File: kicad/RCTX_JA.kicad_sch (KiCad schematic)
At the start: 48 parts

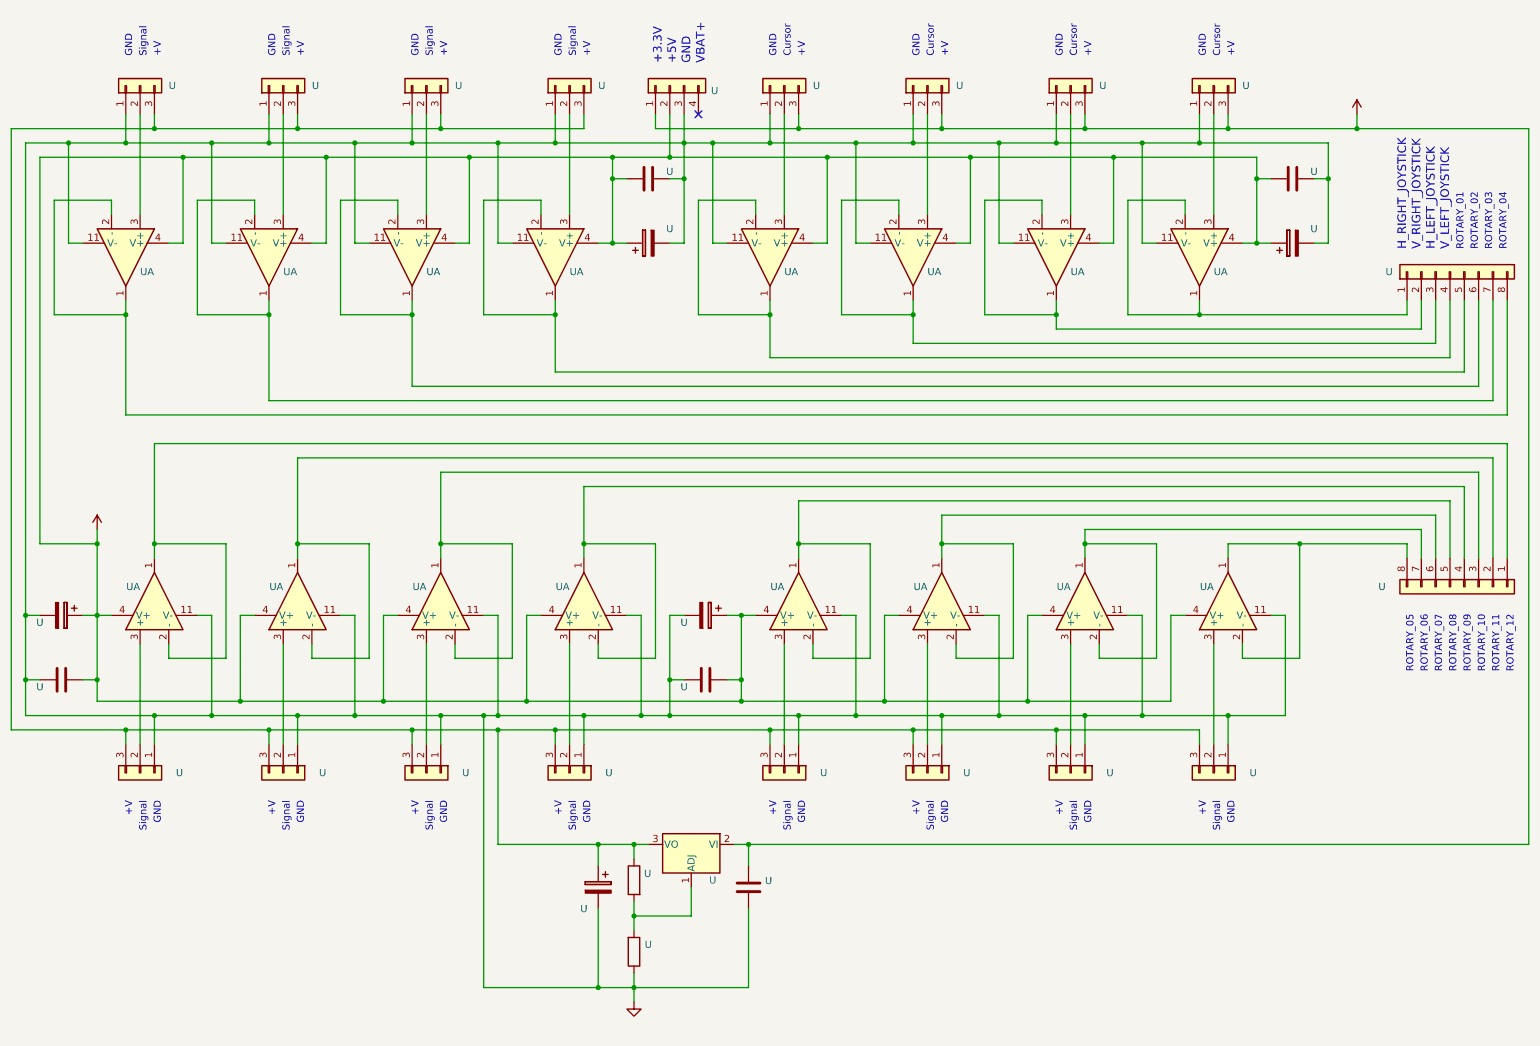
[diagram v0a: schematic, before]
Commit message: Adding PIB USB BRIDGE UML state diagrams - WIP
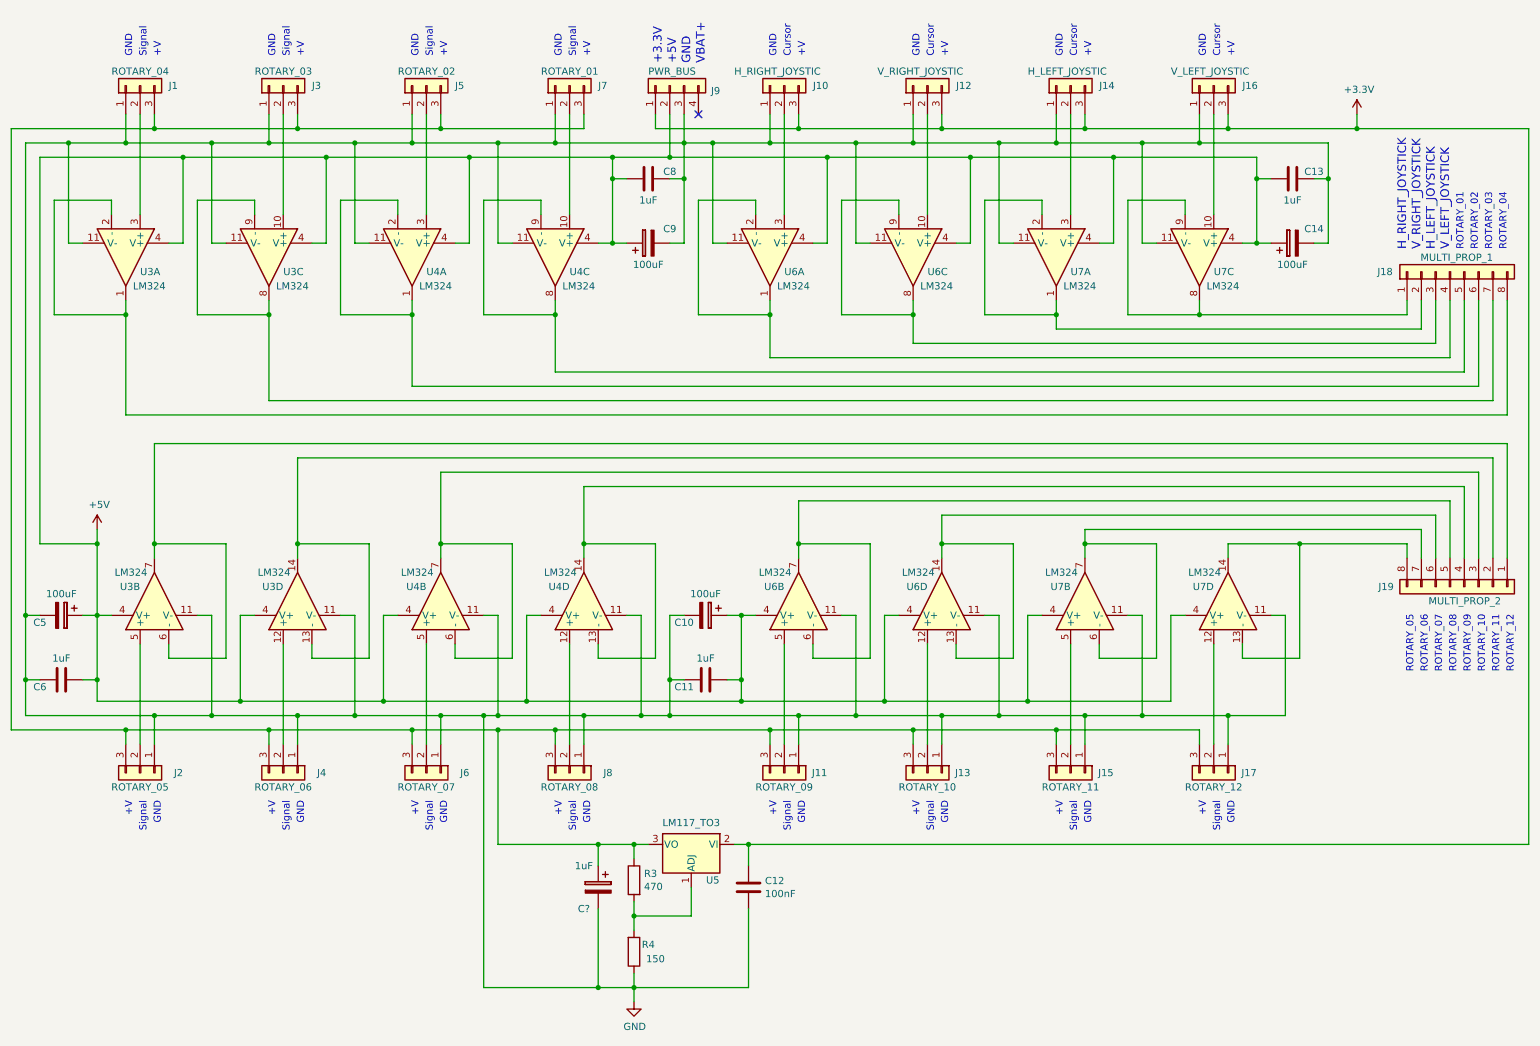
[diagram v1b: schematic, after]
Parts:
- C10, C14, C5, C9: renamed from U; value (none) -> 100uF; footprint (none) -> Capacitors_THT:CP_Radial_D5.0mm_P2.50mm
- C11, C13, C6, C8: renamed from U; value (none) -> 1uF; footprint (none) -> Capacitors_THT:C_Disc_D3.0mm_W1.6mm_P2.50mm
- C12: renamed from U; value (none) -> 100nF; footprint (none) -> Capacitors_THT:C_Disc_D3.0mm_W1.6mm_P2.50mm
- C?: renamed from U; value (none) -> 1uF; footprint (none) -> Capacitors_THT:CP_Radial_D5.0mm_P2.50mm
- J1: renamed from U; value (none) -> ROTARY_04; footprint (none) -> servo_conn:SRV_1
- J10: renamed from U; value (none) -> H_RIGHT_JOYSTIC; footprint (none) -> servo_conn:SRV_1
- J11: renamed from U; value (none) -> ROTARY_09; footprint (none) -> servo_conn:SRV_1
- J12: renamed from U; value (none) -> V_RIGHT_JOYSTIC; footprint (none) -> servo_conn:SRV_1
- J13: renamed from U; value (none) -> ROTARY_10; footprint (none) -> servo_conn:SRV_1
- J14: renamed from U; value (none) -> H_LEFT_JOYSTIC; footprint (none) -> servo_conn:SRV_1
- J15: renamed from U; value (none) -> ROTARY_11; footprint (none) -> servo_conn:SRV_1
- J16: renamed from U; value (none) -> V_LEFT_JOYSTIC; footprint (none) -> servo_conn:SRV_1
- J17: renamed from U; value (none) -> ROTARY_12; footprint (none) -> servo_conn:SRV_1
- J18: renamed from U; value (none) -> MULTI_PROP_1; footprint (none) -> Connectors_Samtec:SL-108-X-XX_1x08
- J19: renamed from U; value (none) -> MULTI_PROP_2; footprint (none) -> Connectors_Samtec:SL-108-X-XX_1x08
- J2: renamed from U; value (none) -> ROTARY_05; footprint (none) -> servo_conn:SRV_1
- J3: renamed from U; value (none) -> ROTARY_03; footprint (none) -> servo_conn:SRV_1
- J4: renamed from U; value (none) -> ROTARY_06; footprint (none) -> servo_conn:SRV_1
- J5: renamed from U; value (none) -> ROTARY_02; footprint (none) -> servo_conn:SRV_1
- J6: renamed from U; value (none) -> ROTARY_07; footprint (none) -> servo_conn:SRV_1
- J7: renamed from U; value (none) -> ROTARY_01; footprint (none) -> servo_conn:SRV_1
- J8: renamed from U; value (none) -> ROTARY_08; footprint (none) -> servo_conn:SRV_1
- J9: renamed from U; value (none) -> PWR_BUS; footprint (none) -> Connectors_Samtec:SL-104-X-XX_1x04
- R3: renamed from U; value (none) -> 470; footprint (none) -> Resistors_THT:R_Axial_DIN0204_L3.6mm_D1.6mm_P1.90mm_Vertical
- R4: renamed from U; value (none) -> 150; footprint (none) -> Resistors_THT:R_Axial_DIN0204_L3.6mm_D1.6mm_P1.90mm_Vertical
- U3, U4, U6, U7: renamed from U; value (none) -> LM324; footprint (none) -> Housings_DIP:DIP-14_W7.62mm
- U5: renamed from U; value (none) -> LM117_TO3; footprint (none) -> TO_SOT_Packages_THT:TO-92_Inline_Narrow_Oval
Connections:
- net at J3.2 (Pin_2): now also U3.10 (+); no longer U3.3 (+)
- net at J7.2 (Pin_2): now also U4.10 (+); no longer U4.3 (+)
- net at J16.2 (Pin_2): now also U7.10 (+); no longer U7.3 (+)
- net at J6.2 (Pin_2): now also U4.5 (+); no longer U4.3 (+)
- net at J4.2 (Pin_2): now also U3.12 (+); no longer U3.3 (+)
- net at J12.2 (Pin_2): now also U6.10 (+); no longer U6.3 (+)
- net at J8.2 (Pin_2): now also U4.12 (+); no longer U4.3 (+)
- net at J2.2 (Pin_2): now also U3.5 (+); no longer U3.3 (+)
- net at J17.2 (Pin_2): now also U7.12 (+); no longer U7.3 (+)
- net at J15.2 (Pin_2): now also U7.5 (+); no longer U7.3 (+)
- net at J13.2 (Pin_2): now also U6.12 (+); no longer U6.3 (+)
- net at J11.2 (Pin_2): now also U6.5 (+); no longer U6.3 (+)
- new net: J18.1 (Pin_1), U7.8, U7.9 (-)
- new net: J18.7 (Pin_7), U3.8, U3.9 (-)
- new net: J18.5 (Pin_5), U4.8, U4.9 (-)
- new net: J18.3 (Pin_3), U6.8, U6.9 (-)
- new net: J19.4 (Pin_4), U4.13 (-), U4.14
- new net: J19.3 (Pin_3), U4.6 (-), U4.7
- new net: J19.2 (Pin_2), U3.13 (-), U3.14
- new net: J19.1 (Pin_1), U3.6 (-), U3.7
- new net: J19.8 (Pin_8), U7.13 (-), U7.14
- new net: J19.7 (Pin_7), U7.6 (-), U7.7
- new net: J19.6 (Pin_6), U6.13 (-), U6.14
- new net: J19.5 (Pin_5), U6.6 (-), U6.7

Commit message: Adding PIB USB BRIDGE UML state diagrams - WIP
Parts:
- gave numbers to parts that had none: 1
